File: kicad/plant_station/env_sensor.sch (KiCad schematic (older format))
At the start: 6 parts, among them IC1 VEML7700-TT, J12 WEATHER_I2C, Q3 DTC113Z, U1 HDC2010YPAT

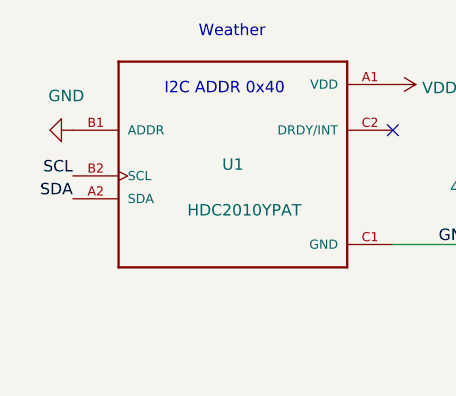
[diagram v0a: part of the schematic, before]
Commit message: v3 PCB in progress. Need to move LED driver to LEDs board and make it connect using the standard interface
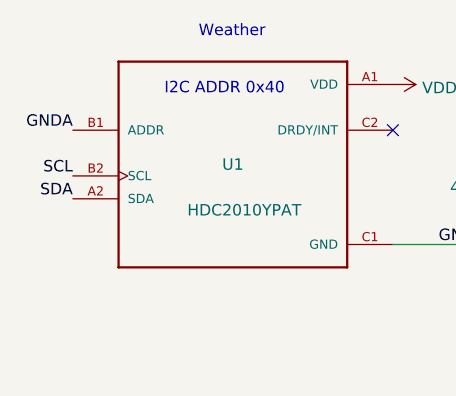
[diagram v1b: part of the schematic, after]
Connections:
- net GND: no longer U1.B1 (ADDR)
- net GNDA: now also U1.B1 (ADDR)
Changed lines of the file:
@@
 Text Label 4300 3250 2    50   ~ 0
 SDA
-$Comp
-L power:GND #PWR?
-U 1 1 605F5D87
-P 4300 2950
-AR Path="/605F5D87" Ref="#PWR?"  Part="1"
-AR Path="/605E9160/605F5D87" Ref="#PWR032"  Part="1"
-F 0 "#PWR032" H 4300 2700 50  0001 C CNN
-F 1 "GND" V 4150 3000 50  0000 R CNN
-F 2 "" H 4300 2950 50  0001 C CNN
-F 3 "" H 4300 2950 50  0001 C CNN
-	1    4300 2950
-	0    1    1    0
-$EndComp
 Text Notes 4700 2800 0    50   ~ 0
 I2C ADDR 0x40
@@
 	1    0    0    -1
 $EndComp
+Text Label 4300 2950 2    50   ~ 0
+GNDA
 $EndSCHEMATC

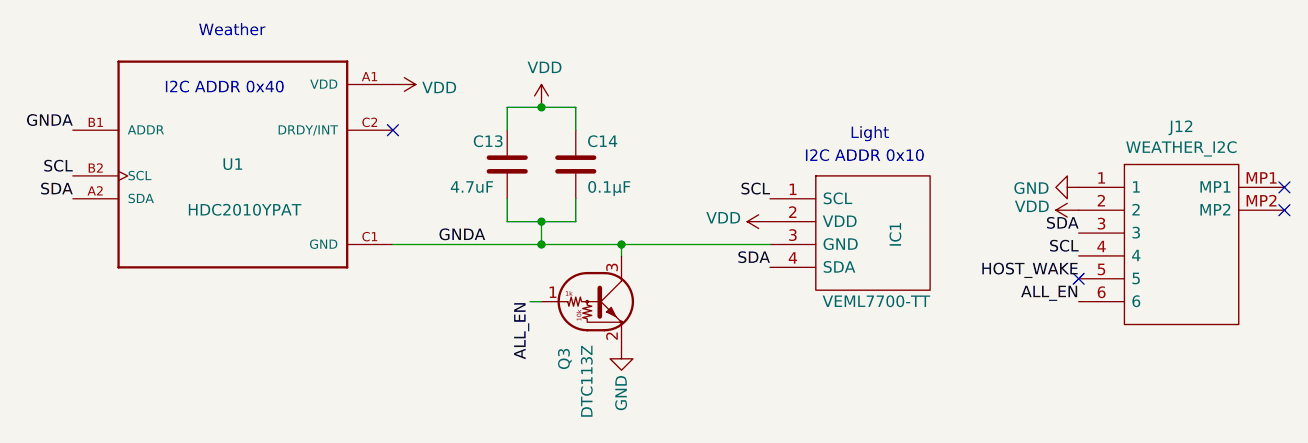
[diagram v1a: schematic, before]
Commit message: Moved the LED driver to LEDs board, refactored connectors. Hopefuly PCBNEW could update it all in place
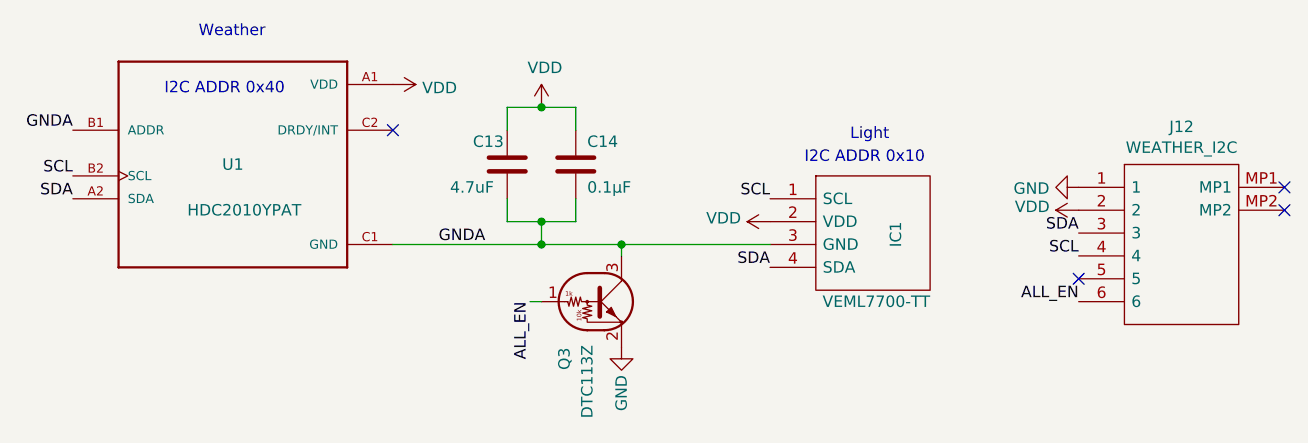
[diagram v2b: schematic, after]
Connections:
- net HOST_WAKE: no longer names the net of J12.5
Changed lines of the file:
@@
 Text Label 8700 3700 2    50   ~ 0
 ALL_EN
-Text Label 8700 3600 2    50   ~ 0
-HOST_WAKE
 $Comp
 L Parts:505567-0671 J?
